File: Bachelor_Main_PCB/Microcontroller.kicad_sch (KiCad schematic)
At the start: 10 parts, among them U3 STM32H7A3ZITxQ, U4 USB3320C-EZK-TR, Y1 SG-210STF 24Mhz

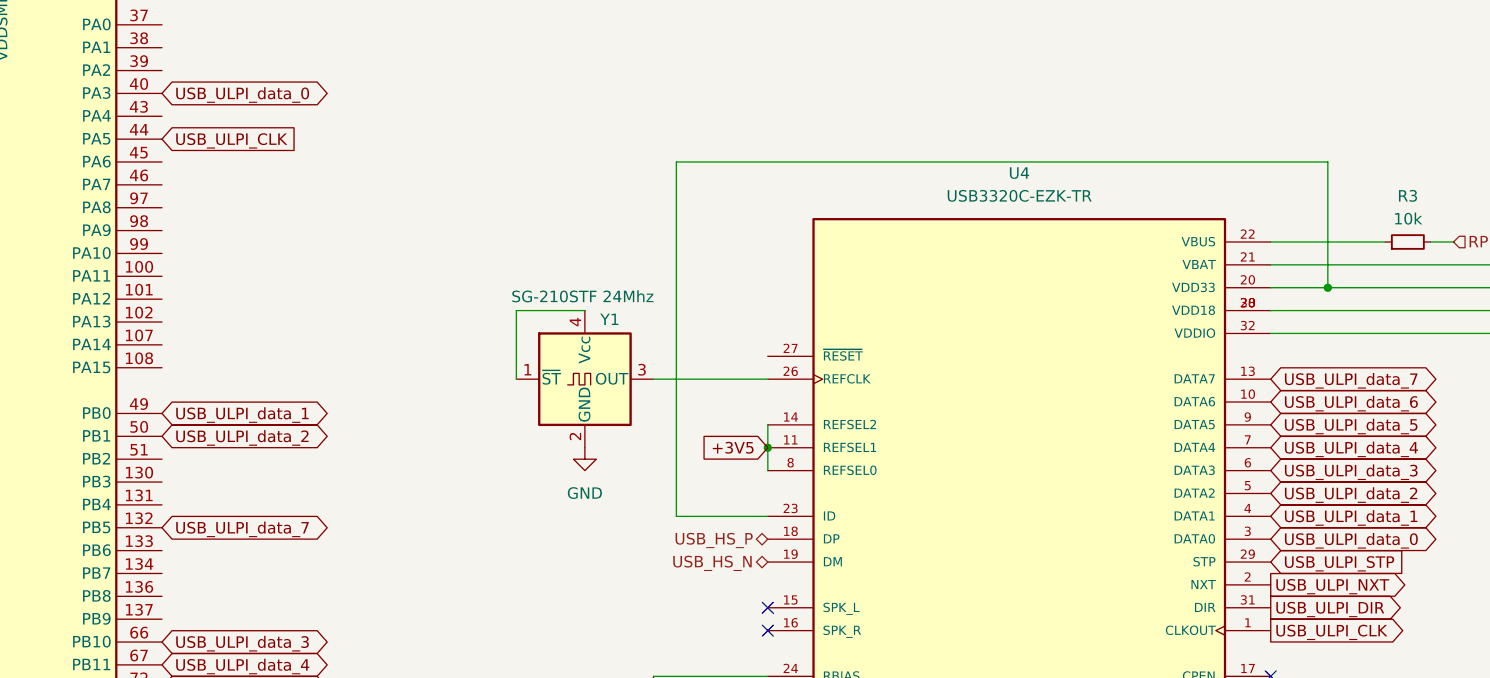
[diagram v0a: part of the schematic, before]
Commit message: Add USB3320 Reset pin pullup
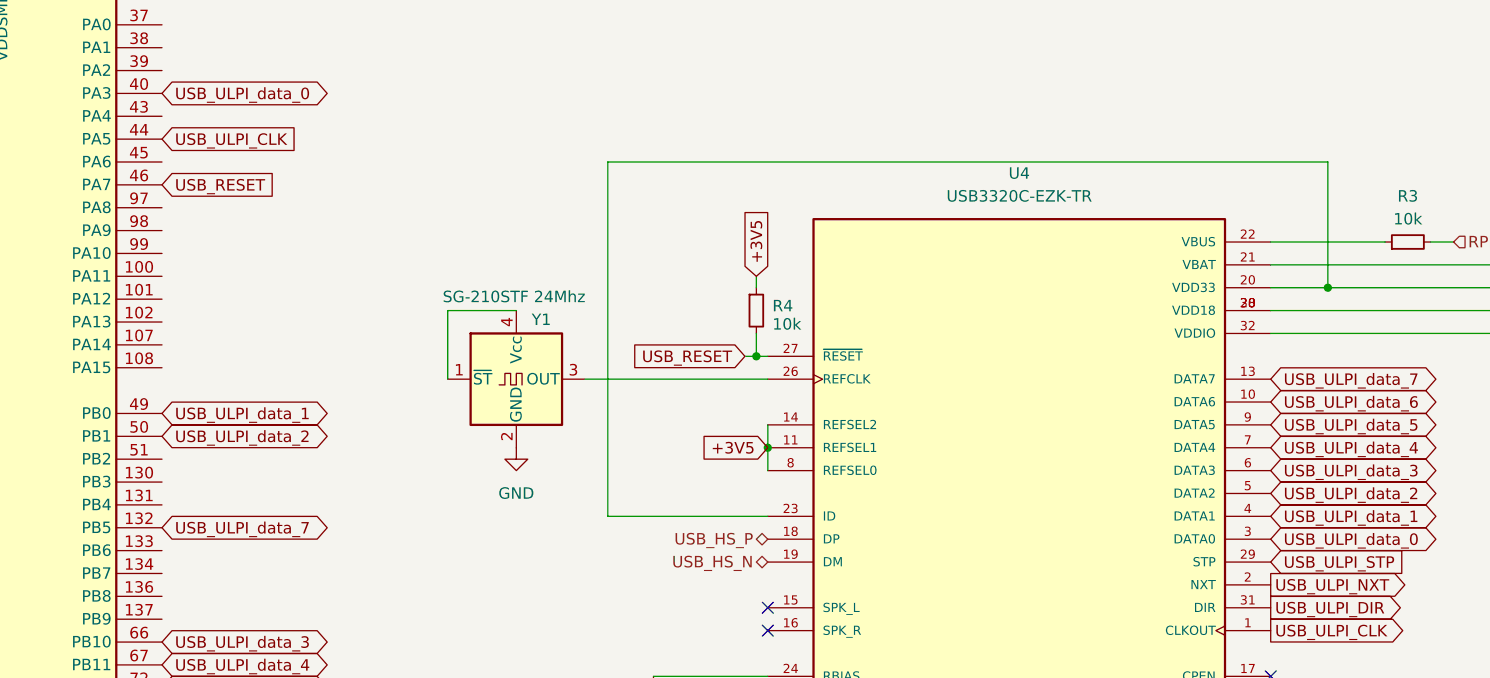
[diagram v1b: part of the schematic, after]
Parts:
- added R4: 10k, Resistor_SMD:R_0603_1608Metric_Pad0.98x0.95mm_HandSolder, symbol Device:R_Small
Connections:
- net +3V5: now also R4.1
- net USB_RESET: now reaches U3.46 (PA7)
- net USB_RESET: now also U4.27 (~{RESET}), R4.2
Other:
- moved on the sheet: Y1
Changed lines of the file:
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@@
 	(paper "A3")
+	(junction
+		(at 209.55 102.87)
+		(diameter 0)
+		(color 0 0 0 0)
+	)
 	(junction
 		(at 92.71 55.88)
@@
 	(wire
 		(pts
-			(xy 210.82 120.65) (xy 200.66 120.65)
+			(xy 209.55 93.98) (xy 209.55 95.25)
+		)
+		(stroke
+			(width 0)
+			(type default)
+		)
+	)
+	(wire
+		(pts
+			(xy 210.82 120.65) (xy 193.04 120.65)
 		)
 		(stroke
@@
 	(wire
 		(pts
+			(xy 210.82 102.87) (xy 209.55 102.87)
+		)
+		(stroke
+			(width 0)
+			(type default)
+		)
+	)
+	(wire
+		(pts
 			(xy 92.71 55.88) (xy 95.25 55.88)
 		)
@@
 	(wire
 		(pts
+			(xy 209.55 100.33) (xy 209.55 102.87)
+		)
+		(stroke
+			(width 0)
+			(type default)
+		)
+	)
+	(wire
+		(pts
 			(xy 273.05 95.25) (xy 317.5 95.25)
 		)
@@
 	(wire
 		(pts
+			(xy 208.28 102.87) (xy 209.55 102.87)
+		)
+		(stroke
+			(width 0)
+			(type default)
+		)
+	)
+	(wire
+		(pts
 			(xy 90.17 55.88) (xy 92.71 55.88)
 		)
@@
 	(wire
 		(pts
-			(xy 200.66 81.28) (xy 200.66 120.65)
+			(xy 193.04 81.28) (xy 193.04 120.65)
 		)
 		(stroke
@@
 	(wire
 		(pts
-			(xy 182.88 105.41) (xy 182.88 97.79)
-		)
-		(stroke
-			(width 0)
-			(type default)
-		)
-	)
-	(wire
-		(pts
-			(xy 198.12 105.41) (xy 210.82 105.41)
-		)
-		(stroke
-			(width 0)
-			(type default)
-		)
-	)
-	(wire
-		(pts
-			(xy 200.66 81.28) (xy 273.05 81.28)
+			(xy 175.26 105.41) (xy 175.26 97.79)
+		)
+		(stroke
+			(width 0)
+			(type default)
+		)
+	)
+	(wire
+		(pts
+			(xy 190.5 105.41) (xy 210.82 105.41)
+		)
+		(stroke
+			(width 0)
+			(type default)
+		)
+	)
+	(wire
+		(pts
+			(xy 193.04 81.28) (xy 273.05 81.28)
 		)
 		(stroke
@@
 	(wire
 		(pts
-			(xy 182.88 97.79) (xy 190.5 97.79)
+			(xy 175.26 97.79) (xy 182.88 97.79)
 		)
 		(stroke
@@
 		)
 	)
+	(global_label "USB_RESET"
+		(shape input)
+		(at 208.28 102.87 180)
+		(fields_autoplaced yes)
+		(effects
+			(font
+				(size 1.27 1.27)
+			)
+			(justify right)
+		)
+		(property "Intersheetrefs" "${INTERSHEET_REFS}"
+			(at 194.7721 102.87 0)
+			(effects
+				(font
+					(size 1.27 1.27)
+				)
+				(justify right)
+				(hide yes)
+			)
+		)
+	)
 	(global_label "USB_ULPI_data_1"
 		(shape bidirectional)
@@
 		)
 	)
+	(global_label "USB_RESET"
+		(shape input)
+		(at 143.51 83.82 0)
+		(fields_autoplaced yes)
+		(effects
+			(font
+				(size 1.27 1.27)
+			)
+			(justify left)
+		)
+		(property "Intersheetrefs" "${INTERSHEET_REFS}"
+			(at 157.0179 83.82 0)
+			(effects
+				(font
+					(size 1.27 1.27)
+				)
+				(justify left)
+				(hide yes)
+			)
+		)
+	)
 	(global_label "USB_ULPI_CLK"
 		(shape output)
@@
 	(global_label "+3V5"
 		(shape input)
+		(at 209.55 93.98 90)
+		(fields_autoplaced yes)
+		(effects
+			(font
+				(size 1.27 1.27)
+			)
+			(justify left)
+		)
+		(property "Intersheetrefs" "${INTERSHEET_REFS}"
+			(at 209.55 85.9148 90)
+			(effects
+				(font
+					(size 1.27 1.27)
+				)
+				(justify left)
+				(hide yes)
+			)
+		)
+	)
+	(global_label "+3V5"
+		(shape input)
 		(at 337.82 92.71 0)
 		(fields_autoplaced yes)
@@
 	(symbol
 		(lib_id "power:GND")
-		(at 190.5 113.03 0)
+		(at 182.88 113.03 0)
 		(unit 1)
 		(exclude_from_sim no)
@@
 		(fields_autoplaced yes)
 		(property "Reference" "#PWR05"
-			(at 190.5 119.38 0)
+			(at 182.88 119.38 0)
 			(effects
 				(font
@@
 		)
 		(property "Value" "GND"
-			(at 190.5 118.11 0)
+			(at 182.88 118.11 0)
 			(effects
 				(font
@@
 		)
 		(property "Footprint" ""
-			(at 190.5 113.03 0)
+			(at 182.88 113.03 0)
 			(effects
 				(font
@@
 		)
 		(property "Datasheet" ""
-			(at 190.5 113.03 0)
+			(at 182.88 113.03 0)
 			(effects
 				(font
@@
 		)
 		(property "Description" "Power symbol creates a global label with name \"GND\" , ground"
-			(at 190.5 113.03 0)
+			(at 182.88 113.03 0)
 			(effects
 				(font
@@
 	)
 	(symbol
+		(lib_id "Device:R_Small")
+		(at 209.55 97.79 0)
+		(unit 1)
+		(exclude_from_sim no)
+		(in_bom yes)
+		(on_board yes)
+		(dnp no)
+		(property "Reference" "R4"
+			(at 211.328 97.282 0)
+			(effects
+				(font
+					(size 1.27 1.27)
+				)
+				(justify left)
+			)
+		)
+		(property "Value" "10k"
+			(at 211.328 99.314 0)
+			(effects
+				(font
+					(size 1.27 1.27)
+				)
+				(justify left)
+			)
+		)
+		(property "Footprint" "Resistor_SMD:R_0603_1608Metric_Pad0.98x0.95mm_HandSolder"
+			(at 209.55 97.79 0)
+			(effects
+				(font
+					(size 1.27 1.27)
+				)
+				(hide yes)
+			)
+		)
+		(property "Datasheet" "~"
+			(at 209.55 97.79 0)
+			(effects
+				(font
+					(size 1.27 1.27)
+				)
+				(hide yes)
+			)
+		)
+		(property "Description" "Resistor, small symbol"
+			(at 209.55 97.79 0)
+			(effects
+				(font
+					(size 1.27 1.27)
+				)
+				(hide yes)
+			)
+		)
+		(pin "1"
+		)
+		(pin "2"
+		)
+		(instances
+			(project "Bachelor_Main_PCB"
+				(path "/3544d663-329e-4884-b753-28436ca187e8/9cdc091d-5c59-45ee-8211-bdd0f330a333"
+					(reference "R4")
+					(unit 1)
+				)
+			)
+		)
+	)
+	(symbol
 		(lib_id "power:GND")
 		(at 198.12 143.51 0)
@@
 	(symbol
 		(lib_id "Oscillator:SG-210STF")
-		(at 190.5 105.41 0)
+		(at 182.88 105.41 0)
 		(unit 1)
 		(exclude_from_sim no)
@@
 		(dnp no)
 		(property "Reference" "Y1"
-			(at 193.294 98.806 0)
+			(at 185.674 98.806 0)
 			(effects
 				(font
@@
 		)
 		(property "Value" "SG-210STF 24Mhz"
-			(at 190.246 96.266 0)
+			(at 182.626 96.266 0)
 			(effects
 				(font
@@
 		)
 		(property "Footprint" "Oscillator:Oscillator_SMD_SeikoEpson_SG210-4Pin_2.5x2.0mm"
-			(at 201.93 114.3 0)
+			(at 194.31 114.3 0)
 			(effects
 				(font
@@
 		)
 		(property "Datasheet" "https://support.epson.biz/td/api/doc_check.php?mode=dl&lang=en&Parts=SG-210STF"
-			(at 187.96 105.41 0)
+			(at 180.34 105.41 0)
 			(effects
 				(font
@@
 		)
 		(property "Description" "CMOS Crystal Oscillator SPXO"
-			(at 190.5 105.41 0)
-			(effects
-				(font
+			(at 182.88 105.41 0)
+			(effects
+				(font

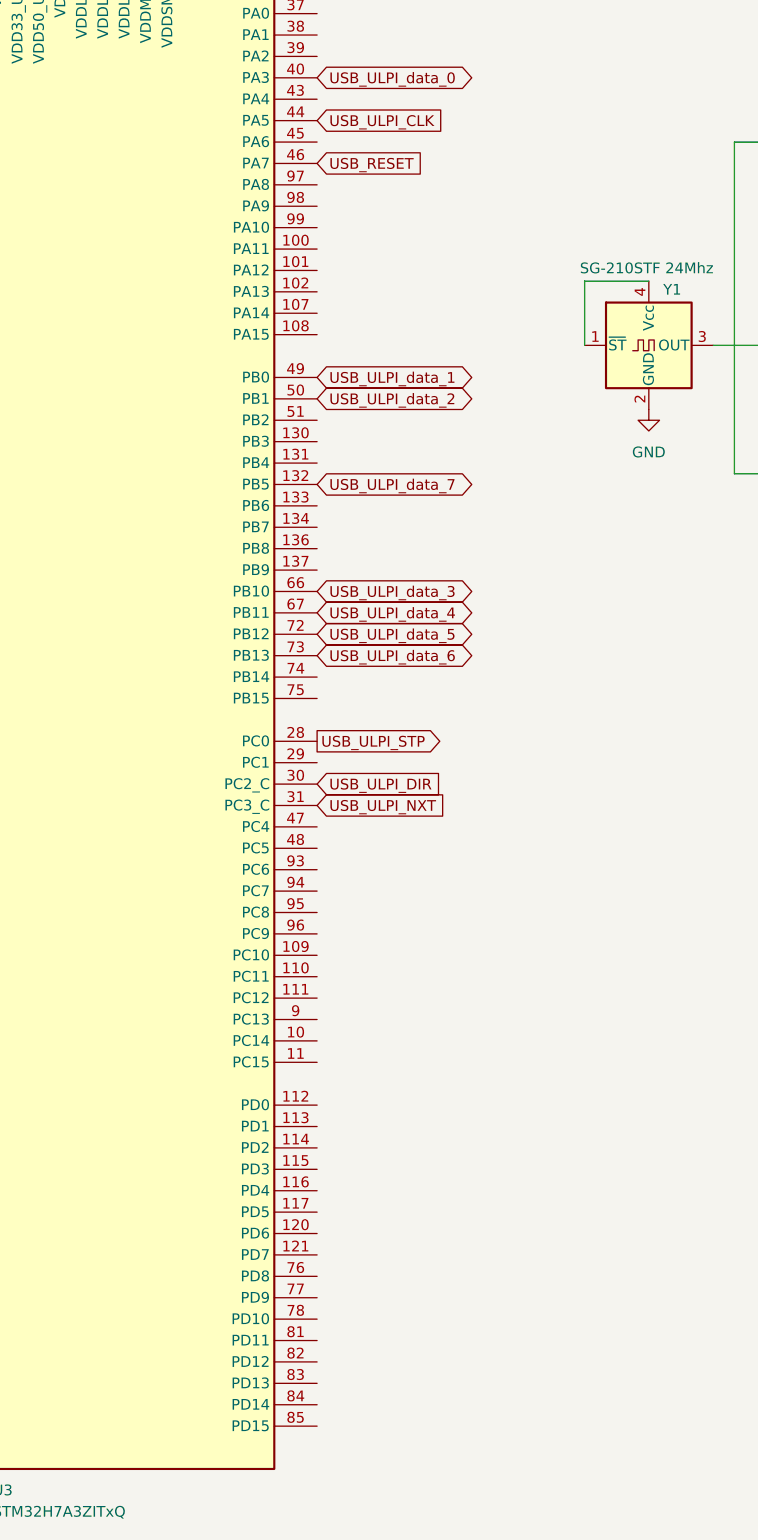
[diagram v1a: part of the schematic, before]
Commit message: USB3320 Reset connected to PD14
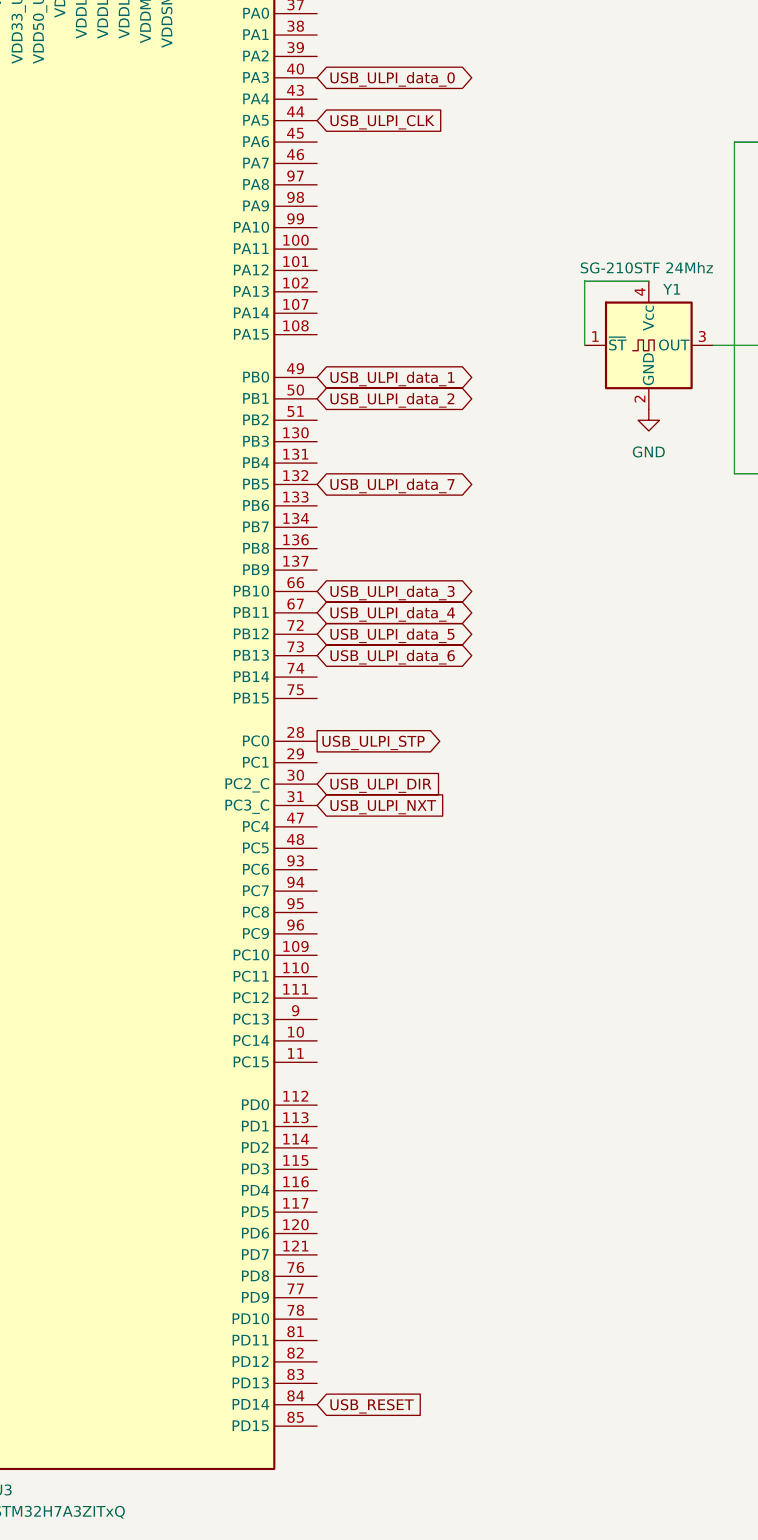
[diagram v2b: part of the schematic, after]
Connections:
- net USB_RESET: now also U3.84 (PD14); no longer U3.46 (PA7)
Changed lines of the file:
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@@
 	(global_label "USB_RESET"
 		(shape input)
-		(at 143.51 83.82 0)
+		(at 143.51 231.14 0)
 		(fields_autoplaced yes)
 		(effects
@@
 		)
 		(property "Intersheetrefs" "${INTERSHEET_REFS}"
-			(at 157.0179 83.82 0)
+			(at 157.0179 231.14 0)
 			(effects
 				(font

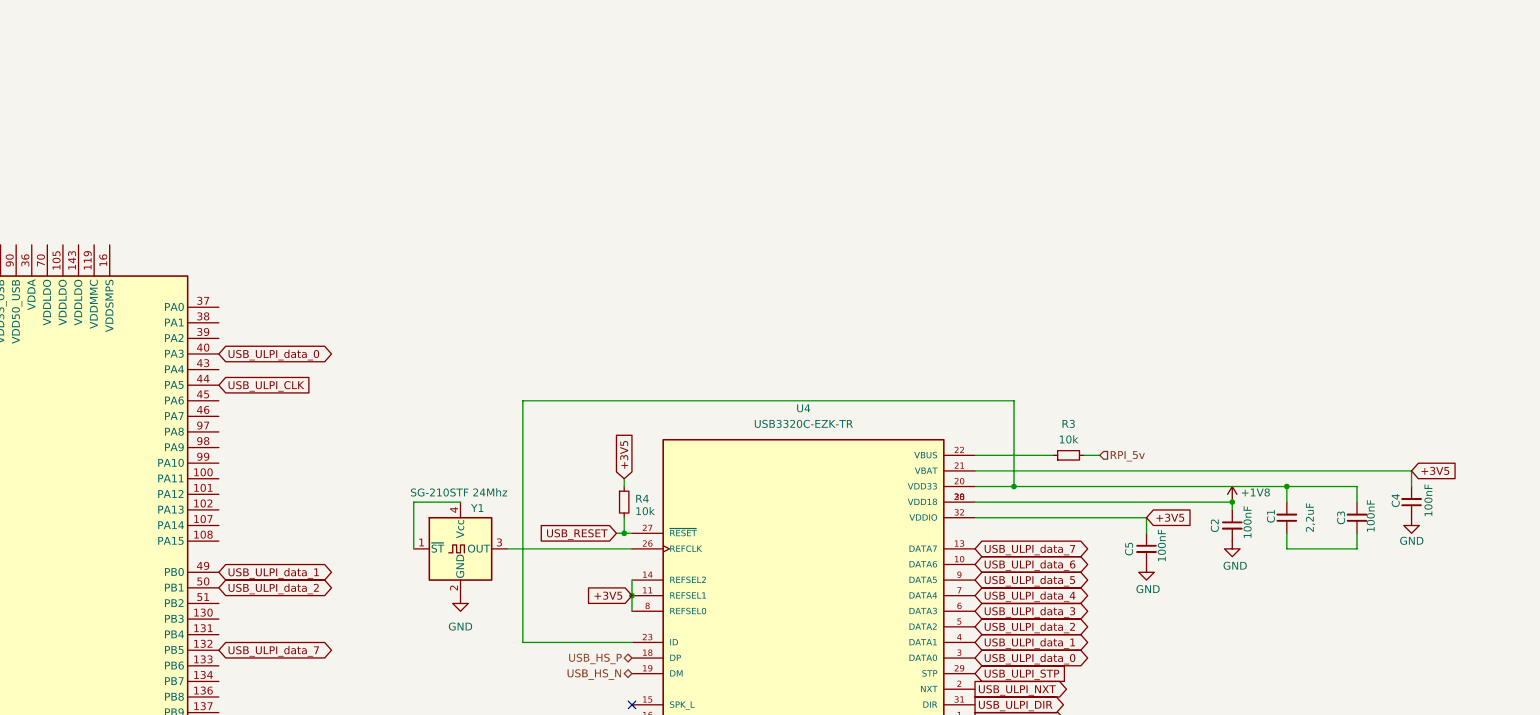
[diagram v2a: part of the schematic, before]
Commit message: Add MCU, USB3320 and USB_HUB power jumpers
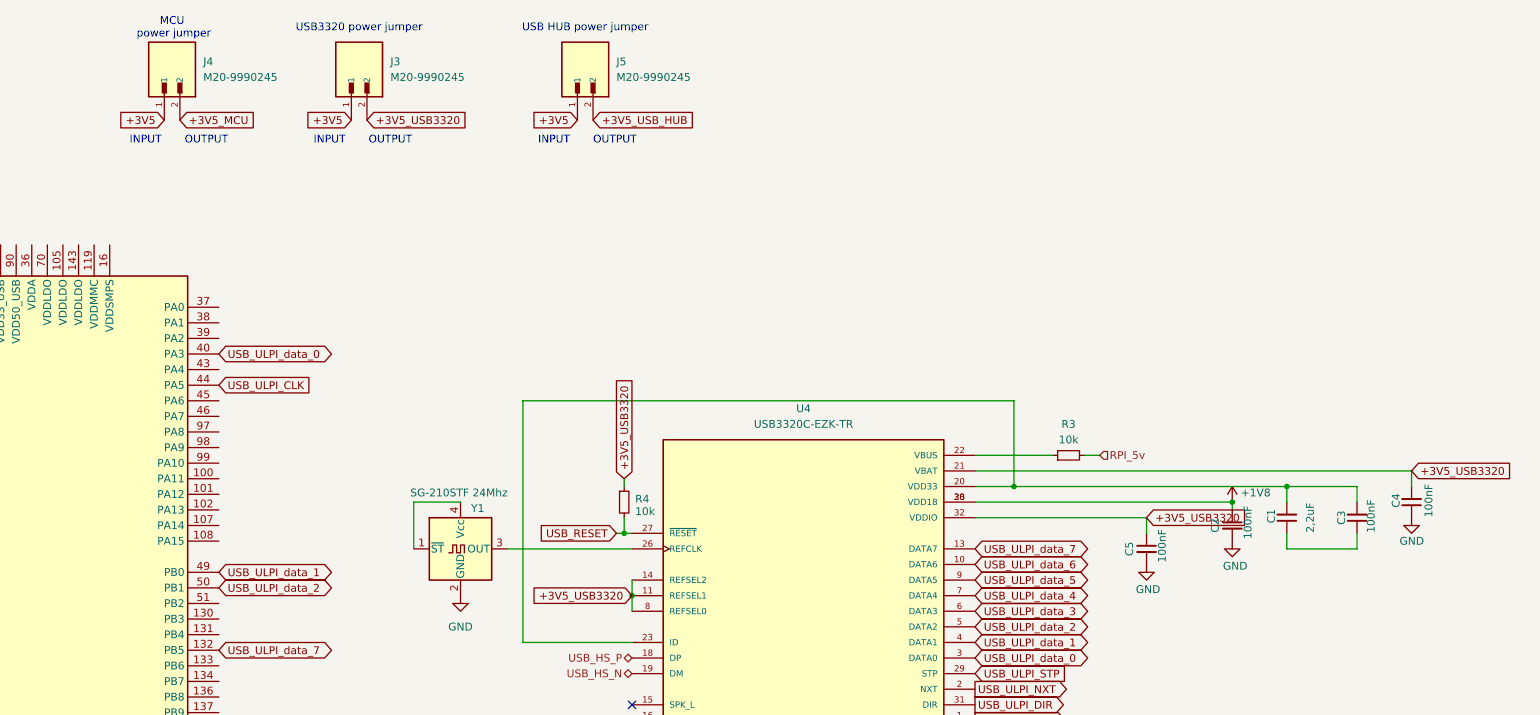
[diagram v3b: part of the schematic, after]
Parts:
- added J3, J4, J5: M20-9990245, M20-9990245:HARWIN_M20-9990245, symbol M20-9990245:M20-9990245
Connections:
- net +3V5: now also J3.1, J4.1, J5.1; no longer C4.2, C5.1, R4.1, U4.11 (REFSEL1), U4.14 (REFSEL2), U4.21 (VBAT), U4.32 (VDDIO), U4.8 (REFSEL0)
- new net +3V5_MCU: J4.2
- new net +3V5_USB3320: C4.2, C5.1, J3.2, R4.1, U4.11 (REFSEL1), U4.14 (REFSEL2), U4.21 (VBAT), U4.32 (VDDIO), U4.8 (REFSEL0)
- new net +3V5_USB_HUB: J5.2
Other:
- note added: "INPUT"
- note added: "MCU power jumper"
- note added: "OUTPUT"
- note added: "USB HUB power jumper"
- note added: "USB3320 power jumper"
